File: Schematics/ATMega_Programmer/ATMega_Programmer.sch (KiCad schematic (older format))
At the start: 10 parts

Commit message: Updates to schematic
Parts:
- added C? (x6): 100nF, symbol Device:C_Small
- added U?: 74HC595, symbol 74xx:74HC595
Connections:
- net BE: now also U?.8; no longer U?.21 (PD7)
- net CLK_DBG: now also U?.19 (PD5); no longer U?.18 (PD4)
- net GND: now also C?.1, C?.2, C?.2, C?.2, C?.2, C?.2, U?.13 (~OE), U?.8 (GND); no longer U?.10, U?.12, U?.13, U?.9
- net SYNC: now also U?.21 (PD7); no longer U?.20 (PD6)
- net VCC: now also C?.1, C?.1, C?.1, C?.1, C?.1, U?.16 (VCC); no longer U?.32 (AREF)
- net ~RES: now also U?.10 (~SRCLR)
- net SR_DAT: now reaches U?.16 (PD2)
- net SR_DAT: now also U?.14 (SER)
- net SR_CLK: now reaches U?.17 (PD3)
- net SR_CLK: now also U?.11 (SRCLK)
- net RDY: now reaches U?.11
- net RW renamed R~W
- net R~W: now also U?.20 (PD6); no longer U?.19 (PD5)
- new net: C?.2, U?.32 (AREF)
- new net BE_CTRL: U?.1 (QB), U?.10, U?.9
- new net CLKSEL: U?.15 (QA)
- new net RDY_CTRL: U?.12, U?.13, U?.2 (QC)
- new net RES_DBG: U?.7 (QH)
- new net SR_OUT: U?.12 (RCLK), U?.18 (PD4)
- no-connect marks 2 -> 1

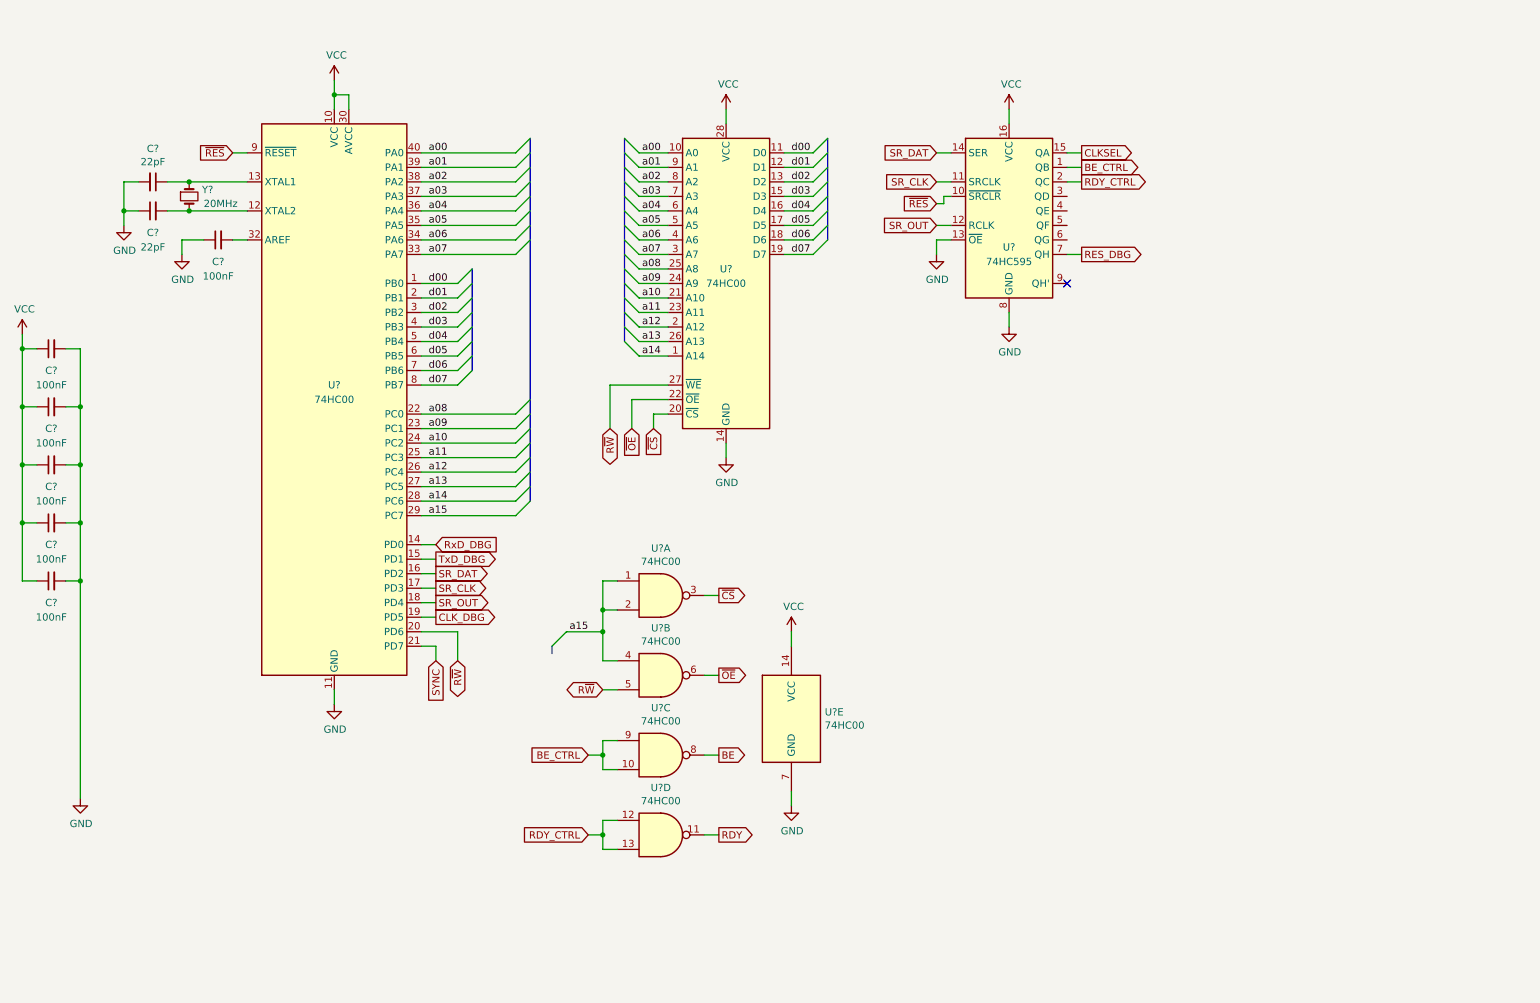
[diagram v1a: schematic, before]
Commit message: Added single gate ICs for clock selection and automatic SR reset
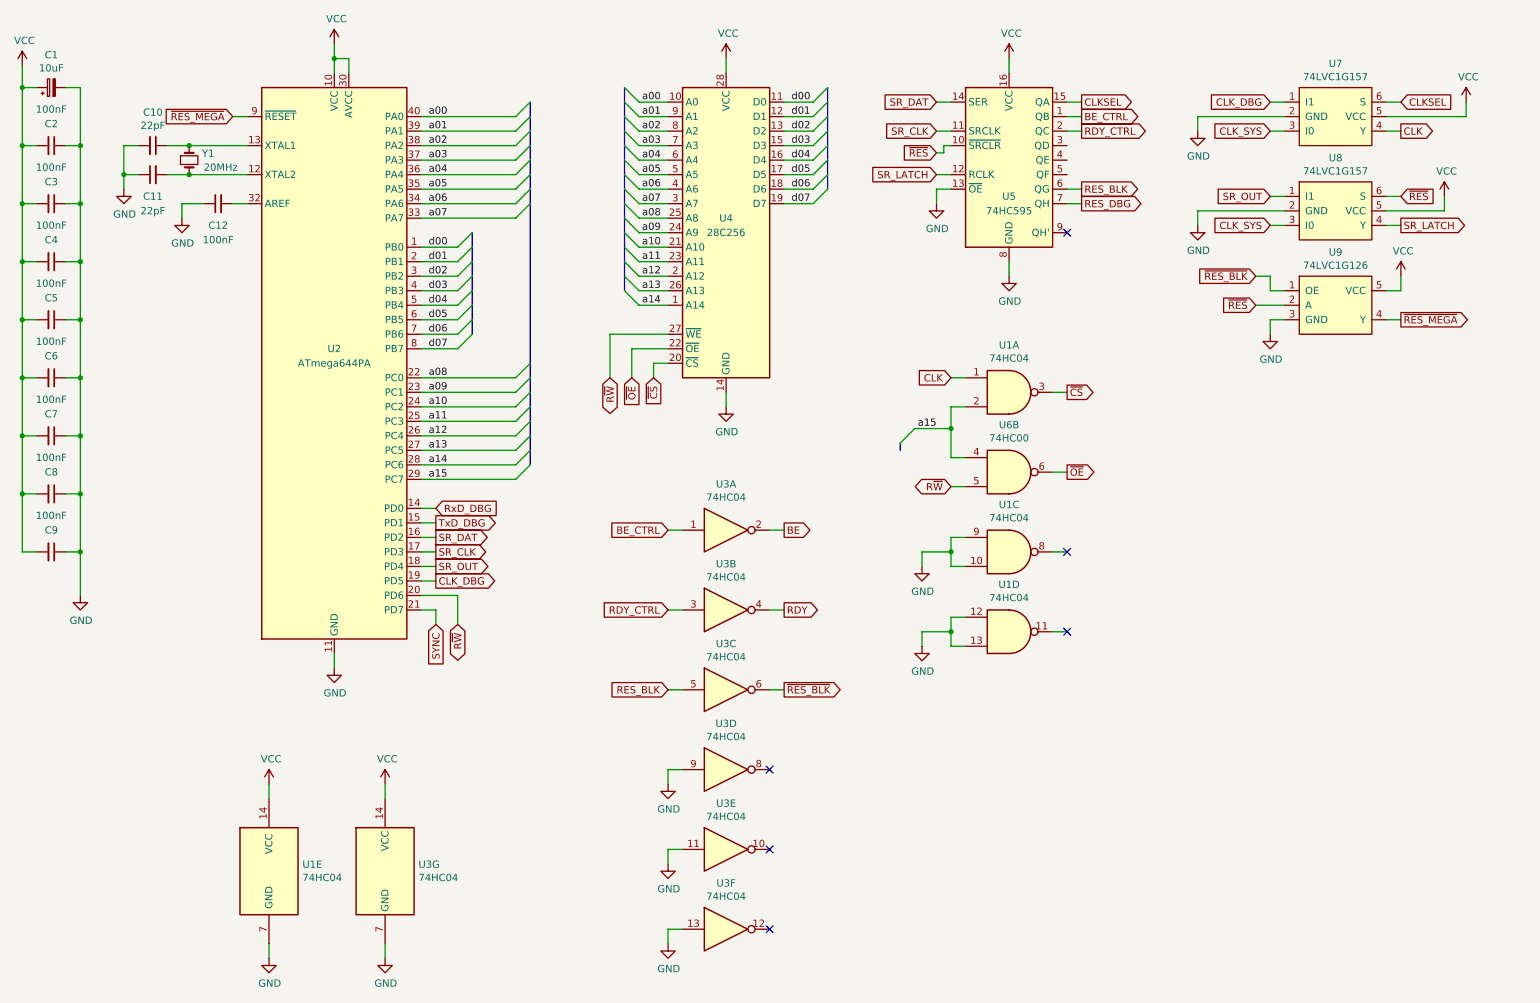
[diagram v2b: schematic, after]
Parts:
- added C1: 10uF, symbol Device:CP_Small
- added C7, C8, C9: 100nF, symbol Device:C_Small
- added U3: 74HC04, symbol 74xx:74HC04
- added U7, U8: 74LVC1G157, Package_SO:SC-74-6_1.5x2.9mm_P0.95mm, symbol 74LVC1G157:74LVC1G157
- added U9: 74LVC1G126, Package_SO:SC-74-6_1.5x2.9mm_P0.95mm, symbol 74LVC1G126:74LVC1G126
- U1: renamed from U?; value 74HC00 -> 74HC04
- U2: renamed from U?; value 74HC00 -> ATmega644PA
- U4: renamed from U?; value 74HC00 -> 28C256
- gave numbers to parts that had none: 11
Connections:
- net BE: now also U3.2; no longer U1.8
- net BE_CTRL: now also U3.1; no longer U1.10, U1.9
- net CLKSEL: now also U7.6 (S)
- net CLK_DBG: now also U7.1 (I1)
- net GND: now also C2.1, C3.1, C4.1, C5.1, C6.1, U1.10, U1.12, U1.13, U1.9, C1.2, C7.1, C8.1, C9.1, U3.11, U3.13, U3.7 (GND), U3.9, U7.2 (GND), U8.2 (GND), U9.3 (GND); no longer C2.2, C3.2, C4.2, C5.2, C6.2
- net RDY: now also U3.4; no longer U1.11
- net RDY_CTRL: now also U3.3; no longer U1.12, U1.13
- net SR_OUT: now also U8.1 (I1); no longer U5.12 (RCLK)
- net VCC: now also C2.2, C3.2, C4.2, C5.2, C6.2, C1.1, C7.2, C8.2, C9.2, U3.14 (VCC), U7.5 (VCC), U8.5 (VCC), U9.5 (VCC); no longer C2.1, C3.1, C4.1, C5.1, C6.1
- net a15: no longer U1.1
- net ~RES: now also U8.6 (S), U9.2 (A); no longer U2.9 (~RESET)
- net RES_BLK: now reaches U5.6 (QG)
- net RES_BLK: now also U3.5
- new net CLK: U1.1, U7.4 (Y)
- new net CLK_SYS: U7.3 (I0), U8.3 (I0)
- new net SR_LATCH: U5.12 (RCLK), U8.4 (Y)
- new net ~RES_BLK: U3.6, U9.1 (OE)
- new net ~RES_MEGA: U2.9 (~RESET), U9.4 (Y)
- no-connect marks 1 -> 6
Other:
- moved on the sheet: C10, C11, C12, C2, C3, C4, C5, C6, U1A, U1C, U1D, U1E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
